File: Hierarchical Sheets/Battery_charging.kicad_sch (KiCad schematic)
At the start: 33 parts, among them J1 USB_C_Receptacle_PowerOnly_6P, J2 Conn_01x01, J3 Conn_01x01, Q1 FS8205A, U1 TP4056-42-ESOP8, U2 DW01A, U3 TPS63060

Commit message: Redo Base Project file add code
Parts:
- renumbered C5 to C10, C6 to C11, C8 to C12, C9 to C3, C1 to C4, C2 to C5, C7 to C6, C10 to C7, C3 to C8, C4 to C9, J2 to J1, J3 to J2, J1 to J3, R10 to R1, R2 to R10, R5 to R2, R6 to R3, R3 to R4, R4 to R5, R7 to R6, R8 to R7, R9 to R8, R1 to R9, U7 to U10, U6 to U11, U1 to U6, U2 to U7, U3 to U9

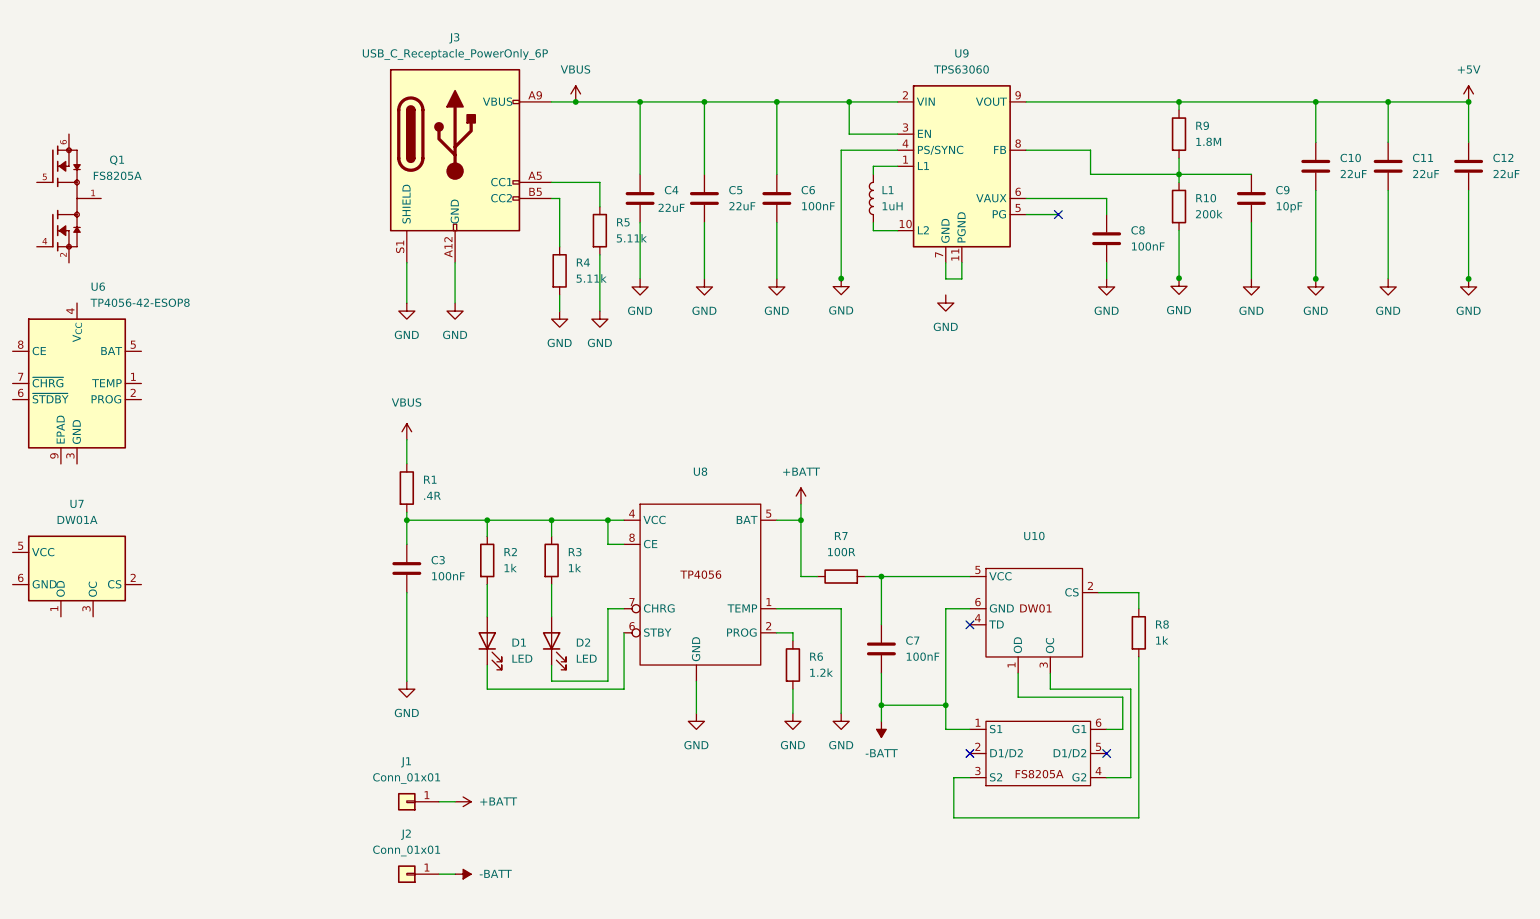
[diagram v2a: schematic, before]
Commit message: Battery Charging Moved
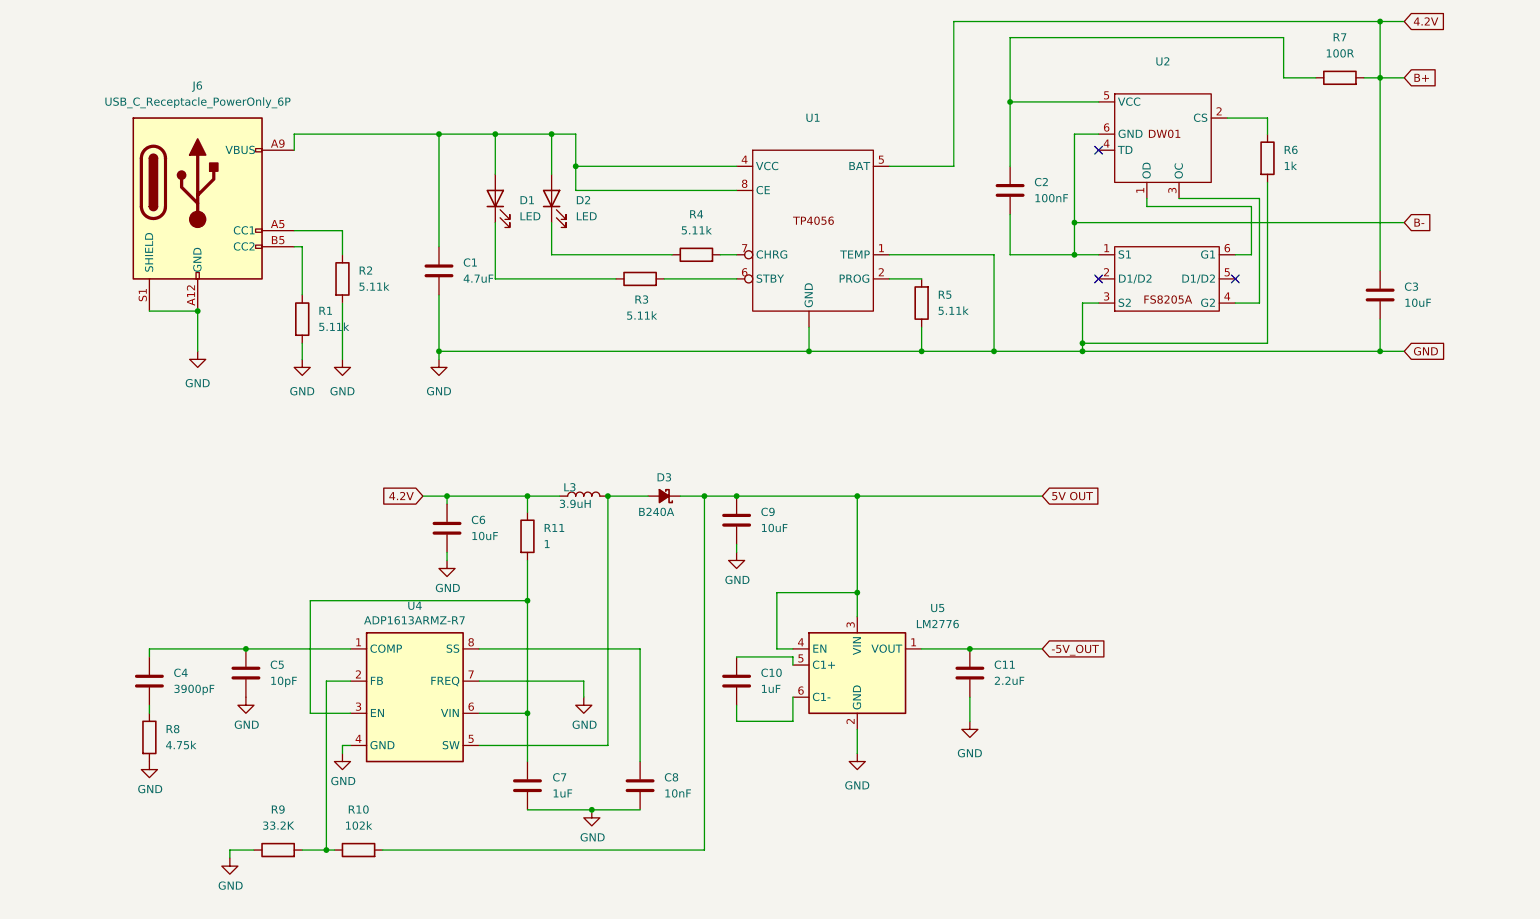
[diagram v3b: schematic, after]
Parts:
- removed C12: 22uF, Capacitor_SMD:C_0805_2012Metric, symbol Device:C
- removed J1, J2: Conn_01x01, symbol Connector_Generic:Conn_01x01
- removed J3: USB_C_Receptacle_PowerOnly_6P, Connector_USB:USB_C_Receptacle_HRO_TYPE-C-31-M-12, symbol Connector:USB_C_Receptacle_PowerOnly_6P
- removed L1: 1uH, Inductor_SMD:L_Coilcraft_XAL4020-XXX, symbol Device:L
- removed Q1: FS8205A, FS8205A:SOP65P640X120-8N, symbol FS8205:FS8205A
- removed U10: ~, symbol TP4056-1:DW01
- removed U11: ~, symbol TP4056-1:FS8205A
- removed U6: TP4056-42-ESOP8, Package_SO:SOIC-8-1EP_3.9x4.9mm_P1.27mm_EP2.41x3.3mm_ThermalVias, symbol Battery_Management:TP4056-42-ESOP8
- removed U7: DW01A, Package_TO_SOT_SMD:SOT-23-6, symbol Battery_Management:DW01A
- removed U8: ~, symbol TP4056-1:TP4056
- removed U9: TPS63060, Package_SON:Texas_S-PWSON-N10_ThermalVias, symbol Regulator_Switching:TPS63060
- added C1: 4.7uF, symbol Device:C
- added C2: 100nF, symbol Device:C
- added D3: B240A, Diode_SMD:D_SMA, symbol Device:D_Schottky_Small_ALT
- added J6: USB_C_Receptacle_PowerOnly_6P, symbol Connector:USB_C_Receptacle_PowerOnly_6P
- added L3: 3.9uH, Inductor_SMD:L_Bourns-SRN4018, symbol Device:L
- added R11: 1, symbol Device:R
- added U1: ~, symbol TP4056-1:TP4056
- added U2: ~, symbol TP4056-1:DW01
- added U3: ~, symbol TP4056-1:FS8205A
- added U4: ADP1613ARMZ-R7, Package_SO:MSOP-8_3x3mm_P0.65mm, symbol Regulator_Switching:ADP1613ARMZ-R7
- added U5: LM2776, Package_TO_SOT_SMD:SOT-23-6, symbol Regulator_SwitchedCapacitor:LM2776
- C10: value 22uF -> 1uF; footprint Capacitor_SMD:C_0805_2012Metric -> (none)
- C11: value 22uF -> 2.2uF; footprint Capacitor_SMD:C_0805_2012Metric -> (none)
- C3: value 100nF -> 10uF
- C4: value 22uF -> 3900pF; footprint Capacitor_SMD:C_0805_2012Metric -> (none)
- C5: value 22uF -> 10pF; footprint Capacitor_SMD:C_0805_2012Metric -> (none)
- C6: value 100nF -> 10uF; footprint Capacitor_SMD:C_0402_1005Metric -> (none)
- C7: value 100nF -> 1uF
- C8: value 100nF -> 10nF; footprint Capacitor_SMD:C_0402_1005Metric -> (none)
- C9: value 10pF -> 10uF; footprint Capacitor_SMD:C_0402_1005Metric -> (none)
- R1: value .4R -> 5.11k; footprint (none) -> Resistor_SMD:R_0402_1005Metric
- R10: value 200k -> 102k; footprint Resistor_SMD:R_0402_1005Metric -> (none)
- R2, R3: value 1k -> 5.11k; footprint (none) -> Resistor_SMD:R_0402_1005Metric
- R6: value 1.2k -> 1k
- R8: value 1k -> 4.75k
- R9: value 1.8M -> 33.2K; footprint Resistor_SMD:R_0402_1005Metric -> (none)
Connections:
- net -BATT is gone; now on net GND: C7.2
- net GND: now also R1.2, R2.2, R5.1, R8.2, R9.1, C1.2, J6.A12 (GND), J6.B12 (GND), J6.S1 (SHIELD), U1. (GND), U1.1 (TEMP), U3.3 (S2), U4.4 (GND), U4.7 (FREQ), U5.2 (GND); no longer C10.2, C4.2, R10.2, R4.2, R5.2
- net at R8.1: now also C4.2
- net at C8.1: now also U4.8 (SS)
- net at R10.1, R9.2: now also U4.2 (FB); no longer C9.1
- net at R6.1: now also U2.2 (CS)
- net at D1.2 (A): now also D2.2 (A), C1.1, J6.A9 (VBUS), J6.B9 (VBUS), U1.4 (VCC), U1.8 (CE); no longer R2.2
- net at D1.1 (K): now also R3.1
- net at D2.1 (K): now also R4.1
- net at R3.2: now also U1.6 (STBY); no longer D2.2 (A)
- net at C7.1: now also R11.2, U4.3 (EN), U4.6 (VIN); no longer R7.2
- removed net +5V: C10.1, C11.1, R9.1
- net +BATT: no longer names the net of R7.1
- net +BATT: now also C2.1, U2.5 (VCC)
- net VBUS: no longer names the net of C4.1, C5.1
- net VBUS: now also U4.1 (COMP); no longer C6.1, R1.1
- new net: R5.2, U1.2 (PROG)
- new net: R4.2, U1.7 (CHRG)
- new net: U2.1 (OD), U3.6 (G1)
- new net: U2.3 (OC), U3.4 (G2)
- new net: J6.B5 (CC2), R1.1
- new net: J6.A5 (CC1), R2.1
- new net: C10.1, U5.5 (C1+)
- new net: C10.2, U5.6 (C1-)
- new net: D3.2 (A), L3.2, U4.5 (SW)
- new net -5V_OUT: C11.1, U5.1 (VOUT)
- new net 4.2V: C3.1, C6.1, L3.1, R11.1, R7.2, U1.5 (BAT)
- new net 5V OUT: C9.1, D3.1 (K), R10.2, U5.3 (VIN), U5.4 (EN)
- new net B-: C2.2, U2.6 (GND), U3.1 (S1)
- no-connect marks 4 -> 3

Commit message: PCB designed rev1.0
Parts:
- added BT1: Battery, Connector_JST:JST_SUR_BM02B-SURS-TF_1x02-1MP_P0.80mm_Vertical, symbol Device:Battery
- C10, C11, C6, C7, C8, C9: footprint (none) -> Capacitor_THT:C_Disc_D3.8mm_W2.6mm_P2.50mm
- C12: renamed from C2; footprint (none) -> Capacitor_THT:C_Disc_D3.8mm_W2.6mm_P2.50mm
- C19: renamed from C3; footprint (none) -> Capacitor_THT:C_Disc_D3.8mm_W2.6mm_P2.50mm
- C3: renamed from C4; footprint (none) -> Capacitor_THT:C_Disc_D3.8mm_W2.6mm_P2.50mm
- C4: renamed from C5; footprint (none) -> Capacitor_THT:C_Disc_D3.8mm_W2.6mm_P2.50mm
- C5: renamed from C1; footprint (none) -> Capacitor_THT:C_Disc_D3.8mm_W2.6mm_P2.50mm
- D1, D2: footprint (none) -> LED_THT:LED_D3.0mm_Horizontal_O1.27mm_Z6.0mm
- J1: renamed from J6; footprint (none) -> Connector_USB:USB_C_Receptacle_GCT_USB4135-GF-A_6P_TopMnt_Horizontal
- R1: renamed from R8; footprint (none) -> Resistor_THT:R_Axial_DIN0204_L3.6mm_D1.6mm_P5.08mm_Horizontal
- R10: renamed from R6; footprint (none) -> Resistor_THT:R_Axial_DIN0204_L3.6mm_D1.6mm_P5.08mm_Horizontal
- R15: renamed from R7; footprint (none) -> Resistor_THT:R_Axial_DIN0204_L3.6mm_D1.6mm_P5.08mm_Horizontal
- R2: renamed from R9; footprint (none) -> Resistor_THT:R_Axial_DIN0204_L3.6mm_D1.6mm_P5.08mm_Horizontal
- R3: renamed from R1; footprint Resistor_SMD:R_0402_1005Metric -> Resistor_THT:R_Axial_DIN0204_L3.6mm_D1.6mm_P5.08mm_Horizontal
- R4: renamed from R2; footprint Resistor_SMD:R_0402_1005Metric -> Resistor_THT:R_Axial_DIN0204_L3.6mm_D1.6mm_P5.08mm_Horizontal
- R5: renamed from R10; footprint (none) -> Resistor_THT:R_Axial_DIN0204_L3.6mm_D1.6mm_P5.08mm_Horizontal
- R6: renamed from R11; footprint (none) -> Resistor_THT:R_Axial_DIN0204_L3.6mm_D1.6mm_P5.08mm_Horizontal
- R7: renamed from R3; footprint Resistor_SMD:R_0402_1005Metric -> Resistor_THT:R_Axial_DIN0204_L3.6mm_D1.6mm_P5.08mm_Horizontal
- R8: renamed from R4; footprint Resistor_SMD:R_0402_1005Metric -> Resistor_THT:R_Axial_DIN0204_L3.6mm_D1.6mm_P5.08mm_Horizontal
- R9: renamed from R5; footprint Resistor_SMD:R_0402_1005Metric -> Resistor_THT:R_Axial_DIN0204_L3.6mm_D1.6mm_P5.08mm_Horizontal
- U10: renamed from U3; footprint (none) -> Package_TO_SOT_SMD:SOT-23-6
- U7: renamed from U1; footprint (none) -> Package_TO_SOT_SMD:SOT-23-8
- U9: renamed from U2; footprint (none) -> Package_TO_SOT_SMD:SOT-23-6
- renumbered D3 to D5, L3 to L1, U4 to U6, U5 to U8
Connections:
- net B-: now also BT1.2 (-)
- net 4.2V renamed B+
- net B+: now also BT1.1 (+)

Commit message: Remove extra ref sensor
each module had a reference sensor before, now have single ref sensor comparing to both sensors
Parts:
- renumbered C5 to C10, C6 to C11, C7 to C12, C8 to C13, C9 to C14, C10 to C15, C11 to C16, C12 to C17, C19 to C18, C3 to C8, C4 to C9, D1 to D3, D2 to D4, R5 to R10, R6 to R11, R7 to R12, R8 to R13, R9 to R14, R10 to R15, R15 to R16, R1 to R6, R2 to R7, R3 to R8, R4 to R9, U9 to U10, U10 to U11, U6 to U7, U7 to U8, U8 to U9

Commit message: Revert "Remove extra ref sensor"
This reverts commit 7f0b0207ac24b991faee57c630f393e10dd69dda.
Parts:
- renumbered C15 to C10, C16 to C11, C17 to C12, C18 to C19, C8 to C3, C9 to C4, C10 to C5, C11 to C6, C12 to C7, C13 to C8, C14 to C9, D3 to D1, D4 to D2, R6 to R1, R15 to R10, R16 to R15, R7 to R2, R8 to R3, R9 to R4, R10 to R5, R11 to R6, R12 to R7, R13 to R8, R14 to R9, U11 to U10, U7 to U6, U8 to U7, U9 to U8, U10 to U9
